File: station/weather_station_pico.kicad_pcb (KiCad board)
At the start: 2 copper layers, 70.4 x 74 mm, 30 parts, among them J1 I2C1_EXP, J2 I2C0_EXP, J3 73412-0110, J4 BME280, J5 WIND_SENSOR, J6 RAIN_SENSOR, J7 SOIL_MOISTURE, J8 SOIL_MOISTURE, J9 Battery Charger, U1 Pico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

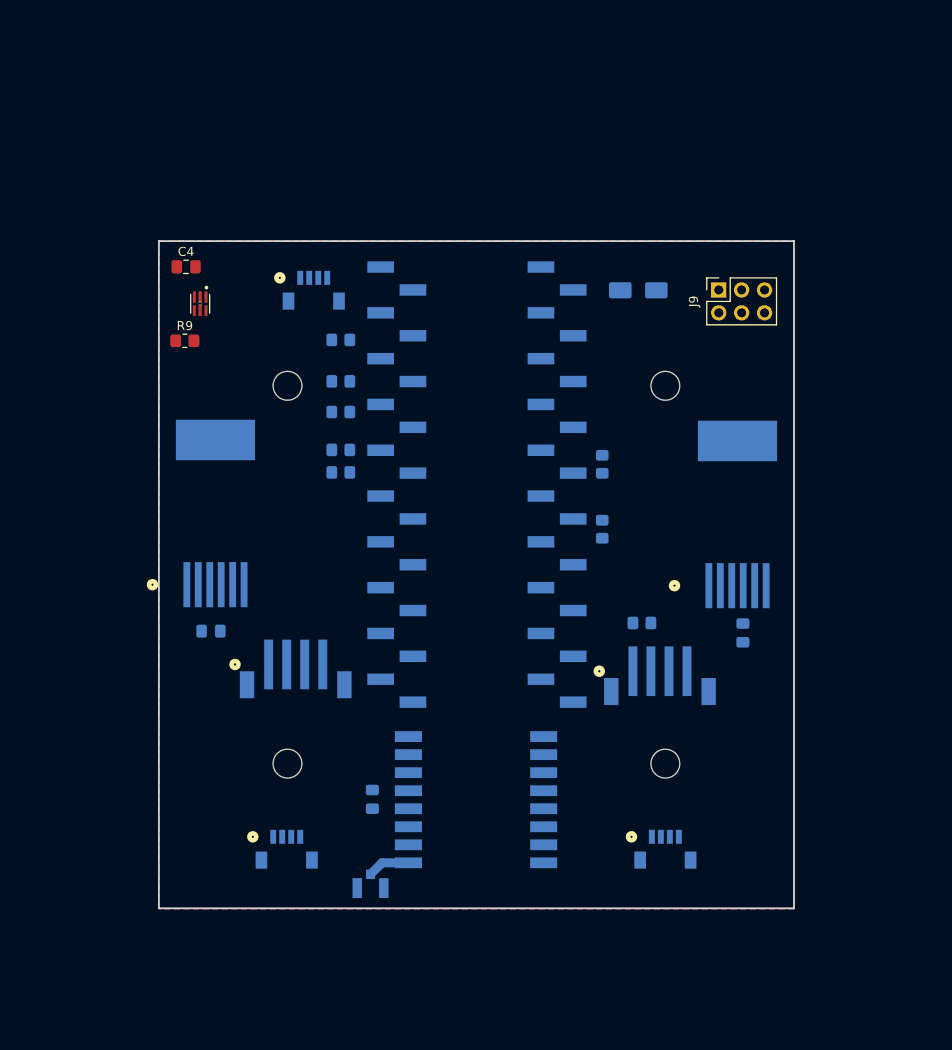
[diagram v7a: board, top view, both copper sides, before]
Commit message: Added a reset button, status LEDs and broke out UART pins
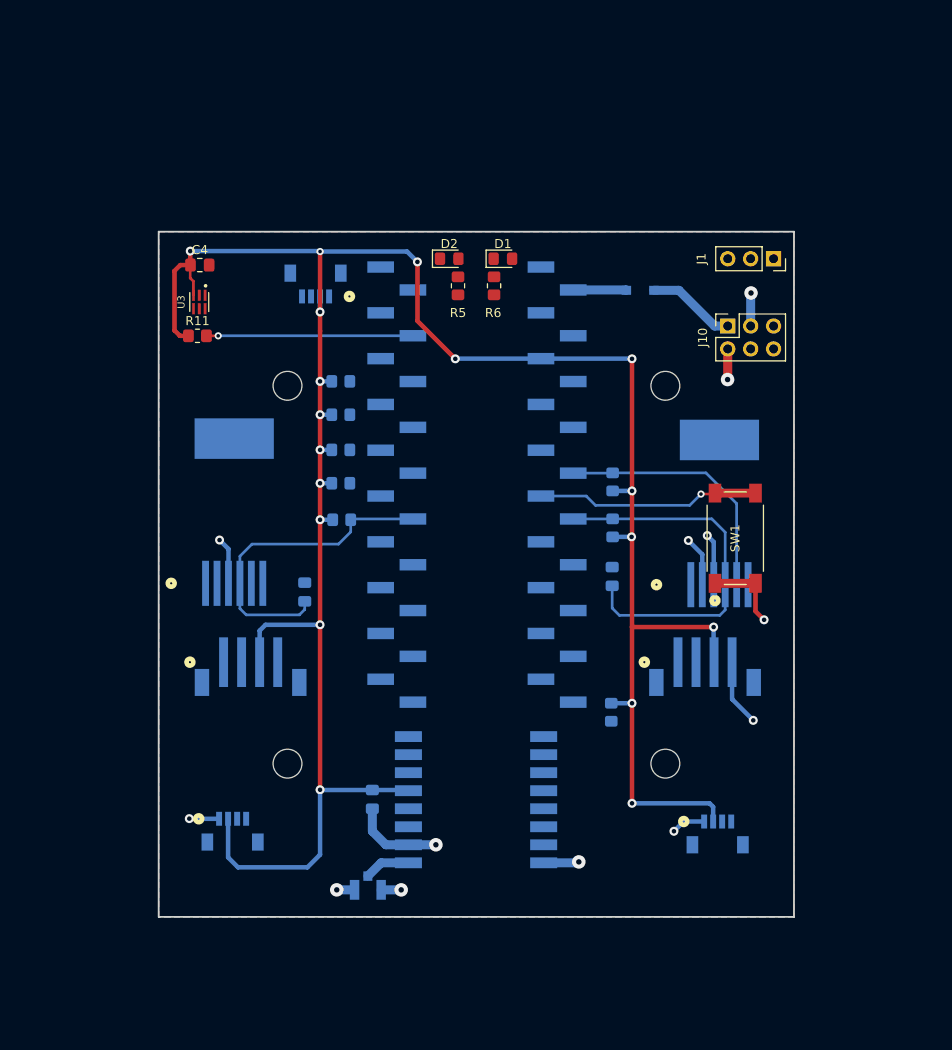
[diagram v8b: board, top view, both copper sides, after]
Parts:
- added CR1: SchottkyDiode, WeatherStation:SchottkyDiode, B.Cu at (165.6, 75.4)
- added D2: RED, LED_SMD:LED_0805_2012Metric_Pad1.15x1.40mm_HandSolder, F.Cu at (144.5, 71.9)
- added J10: Battery Charger, Connector_PinSocket_2.54mm:PinSocket_2x03_P2.54mm_Vertical, F.Cu at (175.4, 79.4)
- added R10: 4.7k, Resistor_SMD:R_0805_2012Metric_Pad1.20x1.40mm_HandSolder, B.Cu at (162.4, 122.2)
- added R11: 10k, Resistor_SMD:R_0805_2012Metric_Pad1.20x1.40mm_HandSolder, F.Cu at (116.5, 80.5)
- added SW1: Reset Button, WeatherStation:TactileButton, F.Cu at (176.2, 102.9)
- D1: value SS12 -> GREEN; footprint Diode_SMD:D_SMA -> LED_SMD:LED_0805_2012Metric_Pad1.15x1.40mm_HandSolder; moved to F.Cu
- J1: value I2C1_EXP -> UART; footprint WeatherStation:StemmaQT_Vertical -> Connector_PinSocket_2.54mm:PinSocket_1x03_P2.54mm_Vertical; moved to F.Cu
- J2: value I2C0_EXP -> I2C1_EXP
- J3: value 73412-0110 -> I2C0_EXP; footprint WeatherStation:Antenna -> WeatherStation:StemmaQT_Vertical
- J4: value BME280 -> 73412-0110; footprint WeatherStation:StemmaQT_Vertical -> WeatherStation:Antenna
- J5: value WIND_SENSOR -> BME280; footprint WeatherStation:RJ11_SMD -> WeatherStation:StemmaQT_Vertical
- J6: value RAIN_SENSOR -> WIND_SENSOR
- J7: value SOIL_MOISTURE -> RAIN_SENSOR; footprint WeatherStation:Stemma_Vertical_Large -> WeatherStation:RJ11_SMD
- J9: value Battery Charger -> SOIL_TEMP; footprint Connector_PinSocket_2.54mm:PinSocket_2x03_P2.54mm_Vertical -> WeatherStation:Stemma_Vertical_Large; moved to B.Cu
- R5, R6: value 10K -> 220; moved to F.Cu
- R8: value 4.7k -> 10K
- R9: value 10k -> 10K; moved to B.Cu
- moved J1 67.1 mm to (180.4, 71.9), turned to -90 degrees
- moved J4 66.3 mm to (135.4, 141.9)
- moved J6 55.9 mm to (174.4, 100.2)
- moved J5 53.6 mm to (129.6, 74.2), turned to 180 degrees
- moved J2 47.8 mm to (174.2, 136.2)
- moved J8 45.4 mm to (122.4, 117.9)
- moved J9 42.6 mm to (172.8, 117.9), turned to 180 degrees
- moved R7 34.0 mm to (162.6, 96.7), turned to 90 degrees
- moved R5 31.4 mm to (145.4, 74.9)
- moved R9 26.4 mm to (132.5, 100.8)
- moved R6 23.2 mm to (149.4, 74.9), turned to 90 degrees
- moved J7 19.4 mm to (120.6, 100.0), turned to 0 degrees
- moved J3 16.4 mm to (120.4, 135.9)
- moved C2 15.8 mm to (162.5, 107.1), turned to 90 degrees
- moved D1 15.4 mm to (150.4, 71.9)
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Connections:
- D1 pad 2: /Battery Charger/Load+ -> /STATUS_LED
- J1 pad 2: +3.3V -> /UART0_RX
- J1 pad 3: /I2C1_SDA -> /UART0_TX
- J2 pad 3: /I2C0_SDA -> /I2C1_SDA
- J2 pad 4: /I2C0_SCL -> /I2C1_SCL
- J3 pad 1: Net-(U2-ANT) -> GND
- J3 pad 2: GND -> +3.3V
- J3 pad 3: (no net) -> /I2C0_SDA
- J4 pad 1: GND -> Net-(U2-ANT)
- J4 pad 2: +3.3V -> GND
- J4 pad 3: /I2C0_SDA -> (no net)
- J5 pad 1: unconnected-(J5-Pad1) -> GND
- J5 pad 2: GND -> +3.3V
- J5 pad 3: GND -> /I2C0_SDA
- J5 pad 4: /WINDSPEED_TGR -> /I2C0_SCL
- J5 pad 5: /WINDDIR_OUT -> (no net)
- J5 pad 6: unconnected-(J5-Pad6) -> (no net)
- J6 pad 2: unconnected-(J6-Pad2) -> GND
- J6 pad 4: /RAIN_COUNT -> /WINDSPEED_TGR
- J6 pad 5: unconnected-(J6-Pad5) -> /WINDDIR_OUT
- J7 pad 1: /I2C0_SCL -> unconnected-(J7-Pad1)
- J7 pad 2: /I2C0_SDA -> unconnected-(J7-Pad2)
- J7 pad 3: +3.3V -> GND
- J7 pad 4: GND -> /RAIN_COUNT
- J7 pad 5: (no net) -> unconnected-(J7-Pad5)
- J7 pad 6: (no net) -> unconnected-(J7-Pad6)
- J8 pad 1: unconnected-(J8-Pin_1-Pad1) -> /I2C0_SCL
- J8 pad 2: /ONE_WIRE -> /I2C0_SDA
- J9 pad 1: /Battery Charger/Load+ -> unconnected-(J9-Pin_1-Pad1)
- J9 pad 2: GND -> /ONE_WIRE
- J9 pad 3: GND -> +3.3V
- J9 pad 4: /Battery Charger/SET -> GND
- J9 pad 5: /Battery Charger/~{FAULT} -> (no net)
- J9 pad 6: /Battery Charger/~{CHRG} -> (no net)
- R5 pad 1: +3.3V -> GND
- R5 pad 2: /WINDDIR_OUT -> Net-(D1-K)
- R6 pad 1: +3.3V -> GND
- R6 pad 2: /WINDSPEED_TGR -> Net-(D2-K)
- R7 pad 2: /RAIN_COUNT -> /WINDDIR_OUT
- R8 pad 1: /ONE_WIRE -> +3.3V
- R8 pad 2: +3.3V -> /WINDSPEED_TGR
- R9 pad 2: /LIGHT_INTR -> /RAIN_COUNT
- U1 pad 1: unconnected-(U1-GP0-Pad1) -> /UART0_TX
- U1 pad 12: unconnected-(U1-GP9-Pad12) -> /RAIN_COUNT
- U1 pad 2: unconnected-(U1-GP1-Pad2) -> /UART0_RX
- U1 pad 20: /LIGHT_INTR -> unconnected-(U1-GP15-Pad20)
- U1 pad 29: /WINDDIR_OUT -> /WINDSPEED_TGR
- U1 pad 30: unconnected-(U1-~{RUN}-Pad30) -> /RESET
- U1 pad 31: /WINDSPEED_TGR -> /WINDDIR_OUT
- U1 pad 32: unconnected-(U1-GP27-Pad32) -> /STATUS_LED
- U1 pad 34: unconnected-(U1-GP28-Pad34) -> /ERROR_LED
- U1 pad 39: Net-(D1-K) -> Net-(U1-VSYS)
- U1 pad 4: unconnected-(U1-GP2-Pad4) -> /LIGHT_INTR
- U1 pad 5: /RAIN_COUNT -> unconnected-(U1-GP3-Pad5)
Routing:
- net +3.3V: track 0.00 -> 264.0 mm, vias 0 -> 18
- net GND: track 0.00 -> 65.4 mm, vias 0 -> 13
- net /WINDSPEED_TGR: track 0.00 -> 41.7 mm
- net /RAIN_COUNT: track 0.00 -> 36.1 mm
- net /WINDDIR_OUT: track 0.00 -> 28.5 mm
- net /RESET: track 0.00 -> 24.8 mm, vias 0 -> 1
- net /LIGHT_INTR: track 0.00 -> 22.9 mm, vias 0 -> 1
- net /Battery Charger/Load+: track 0.00 -> 9.83 mm
- net Net-(U1-VSYS): track 0.00 -> 5.91 mm
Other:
- board size 70.4 x 74 mm -> 70.5 x 76 mm
- rule pad_to_mask_clearance: 0 -> 0.0508
